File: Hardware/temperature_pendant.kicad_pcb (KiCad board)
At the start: 2 copper layers, 26.7 x 24.1 mm, 5 parts, among them J1 CONN-6, SW1 SW-MOM, U1 BLINKM/MINM, U2 TMP3X

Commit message: Added drill hole
Added a mechanical hole that could be used for chain for the pendant.
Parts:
- added MECH-HOLE220: VAL**, MECH-HOLE220, F.Cu at (213.4, 125.7)
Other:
- board size 26.7 x 24.1 mm -> 26.7 x 27.9 mm
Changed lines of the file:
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@@
     (area 199.339999 118.876 226.559 151.180001)
     (thickness 1.6)
-    (drawings 6)
+    (drawings 10)
     (tracks 36)
     (zones 0)
-    (modules 5)
+    (modules 6)
     (nets 7)
   )
@@
     )
   )
+  (module MECH-HOLE220 (layer F.Cu)
+    (at 213.36 125.73)
+    (fp_text reference MECH-HOLE220 (at 0 0) (layer F.SilkS) hide
+      (effects (font (size 1 1) (thickness 0.15)))
+    )
+    (fp_text value VAL** (at 0 0) (layer F.SilkS) hide
+      (effects (font (size 1 1) (thickness 0.15)))
+    )
+    (fp_circle (center 0 0) (end 2.5 0) (layer F.SilkS) (width 0.15))
+    (pad "" thru_hole circle (at 0 0) (size 2.8 2.8) (drill 2.2)
+      (layers *.Cu *.Mask F.SilkS)
+    )
+  )
+  (gr_line (start 199.39 123.19) (end 199.39 124.46) (angle 90) (layer Edge.Cuts) (width 0.1))
+  (gr_line (start 226.06 123.19) (end 226.06 124.46) (angle 90) (layer Edge.Cuts) (width 0.1))
+  (gr_line (start 199.39 124.46) (end 199.39 127) (angle 90) (layer Edge.Cuts) (width 0.1))
+  (gr_line (start 226.06 127) (end 226.06 124.46) (angle 90) (layer Edge.Cuts) (width 0.1))
   (gr_text "Matthew Nelson\n2013" (at 219.71 137.16) (layer F.SilkS)
     (effects (font (size 1 1) (thickness 0.25)))
@@
   (gr_line (start 226.06 151.13) (end 199.39 151.13) (angle 90) (layer Edge.Cuts) (width 0.1))
   (gr_line (start 226.06 127) (end 226.06 151.13) (angle 90) (layer Edge.Cuts) (width 0.1))
-  (gr_line (start 199.39 127) (end 226.06 127) (angle 90) (layer Edge.Cuts) (width 0.1))
+  (gr_line (start 199.39 123.19) (end 226.06 123.19) (angle 90) (layer Edge.Cuts) (width 0.1))
   (segment (start 222.78 135.345) (end 222.78 135.7981) (width 0.254) (layer F.Cu) (net 1))
   (segment (start 222.78 135.7981) (end 222.78 136.2513) (width 0.254) (layer F.Cu) (net 1))

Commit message: Fixed sensor, added locking connector
Fixed the backward wiring on the sensor, added locking connector.  Fixes
issue #4 for the sensor and issue #3 for the locking connector.
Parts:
- removed MECH-HOLE220: VAL**, MECH-HOLE220
- J1: footprint HDRV6W38P254_6X1 -> HDRV5W38P254_6X1-LOCK
- U2: footprint TO92 -> TO92-INVERT
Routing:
- net +BATT: track 53.2 -> 44.6 mm
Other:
- board text added: "Temp Pendant r2"
- board text removed: "Temp Pendant r1"

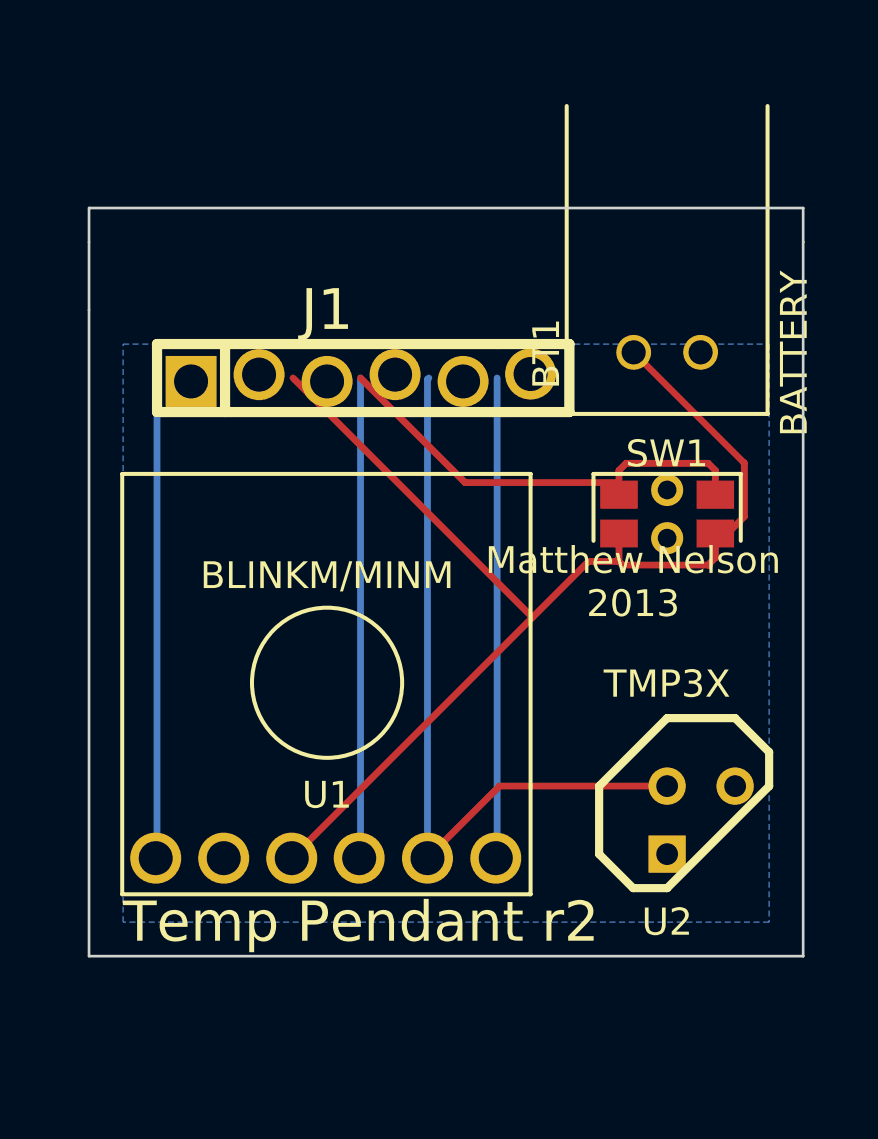
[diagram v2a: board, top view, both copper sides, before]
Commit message: Minor change cleanup
Moved switch and battery connector.  Cleaned up tracks in preparation
for a redo on the layout.
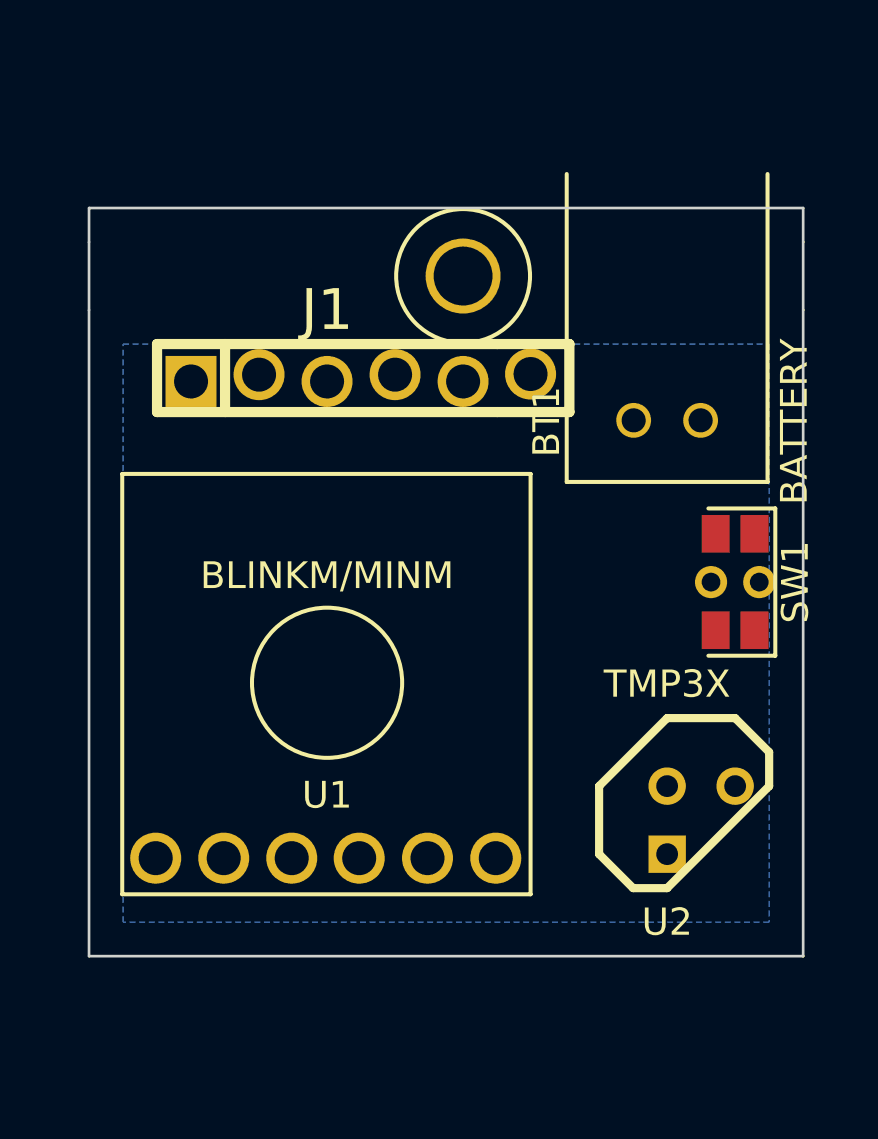
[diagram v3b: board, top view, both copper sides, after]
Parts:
- added MECH-HOLE220: VAL**, MECH-HOLE220, F.Cu at (213.4, 125.7)
- moved SW1 3.59 mm to (223.5, 137.2), turned to 270 degrees
- moved BT1 2.54 mm to (221.0, 121.9)
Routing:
- net +BATT: track 44.6 -> 0.00 mm
- net SW: track 34.8 -> 0.00 mm
- net TEMP: track 28.0 -> 0.00 mm
- net RST: track 18.0 -> 0.00 mm
- net MISO: track 18.0 -> 0.00 mm
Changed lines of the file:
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@@
   (general
     (links 15)
-    (no_connects 9)
+    (no_connects 12)
     (area 199.339999 118.876 226.559 151.180001)
     (thickness 1.6)
     (drawings 10)
-    (tracks 33)
+    (tracks 0)
     (zones 0)
-    (modules 5)
+    (modules 6)
     (nets 7)
   )
@@
   )
   (module CONN-JST-XH-2 (layer F.Cu)
-    (at 220.98 119.38)
+    (at 220.98 121.92)
     (fp_text reference BT1 (at -4.5 9.25 90) (layer F.SilkS)
       (effects (font (size 1 1) (thickness 0.15)))
@@
   )
   (module SW-EVQP7 (layer F.Cu)
-    (at 220.98 134.62)
+    (at 223.52 137.16 270)
     (descr "SW, Mom, SMD Right")
-    (fp_text reference SW1 (at 0 -2.25) (layer F.SilkS)
-      (effects (font (size 1 1) (thickness 0.15)))
-    )
-    (fp_text value SW-MOM (at 0 0) (layer F.SilkS) hide
+    (fp_text reference SW1 (at 0 -2.25 270) (layer F.SilkS)
+      (effects (font (size 1 1) (thickness 0.15)))
+    )
+    (fp_text value SW-MOM (at 0 0 270) (layer F.SilkS) hide
       (effects (font (size 1 1) (thickness 0.15)))
     )
@@
     (fp_line (start -2.75 -1.5) (end 2.75 -1.5) (layer F.SilkS) (width 0.15))
     (fp_line (start 2.75 -1.5) (end 2.75 1) (layer F.SilkS) (width 0.15))
-    (pad 1 smd rect (at 1.8 -0.725) (size 1.4 1.05)
+    (pad 1 smd rect (at 1.8 -0.725 270) (size 1.4 1.05)
       (layers F.Cu F.Paste F.Mask)
       (net 5 SW)
     )
-    (pad 1 smd rect (at -1.8 -0.725) (size 1.4 1.05)
+    (pad 1 smd rect (at -1.8 -0.725 270) (size 1.4 1.05)
       (layers F.Cu F.Paste F.Mask)
       (net 5 SW)
     )
-    (pad 2 smd rect (at -1.8 0.725) (size 1.4 1.05)
+    (pad 2 smd rect (at -1.8 0.725 270) (size 1.4 1.05)
       (layers F.Cu F.Paste F.Mask)
       (net 1 +BATT)
     )
-    (pad 2 smd rect (at 1.8 0.725) (size 1.4 1.05)
+    (pad 2 smd rect (at 1.8 0.725 270) (size 1.4 1.05)
       (layers F.Cu F.Paste F.Mask)
       (net 1 +BATT)
     )
-    (pad "" thru_hole circle (at 0 -0.9) (size 1.2 1.2) (drill 0.7)
-      (layers *.Cu *.Mask F.SilkS)
-    )
-    (pad "" thru_hole circle (at 0 0.9) (size 1.2 1.2) (drill 0.7)
+    (pad "" thru_hole circle (at 0 -0.9 270) (size 1.2 1.2) (drill 0.7)
+      (layers *.Cu *.Mask F.SilkS)
+    )
+    (pad "" thru_hole circle (at 0 0.9 270) (size 1.2 1.2) (drill 0.7)
       (layers *.Cu *.Mask F.SilkS)
     )
@@
     )
   )
+  (module MECH-HOLE220 (layer F.Cu)
+    (at 213.36 125.73)
+    (fp_text reference MECH-HOLE220 (at 0 0) (layer F.SilkS) hide
+      (effects (font (size 1 1) (thickness 0.15)))
+    )
+    (fp_text value VAL** (at 0 0) (layer F.SilkS) hide
+      (effects (font (size 1 1) (thickness 0.15)))
+    )
+    (fp_circle (center 0 0) (end 2.5 0) (layer F.SilkS) (width 0.15))
+    (pad "" thru_hole circle (at 0 0) (size 2.8 2.8) (drill 2.2)
+      (layers *.Cu *.Mask F.SilkS)
+    )
+  )
   (gr_line (start 199.39 123.19) (end 199.39 124.46) (angle 90) (layer Edge.Cuts) (width 0.1))
   (gr_line (start 226.06 123.19) (end 226.06 124.46) (angle 90) (layer Edge.Cuts) (width 0.1))
   (gr_line (start 199.39 124.46) (end 199.39 127) (angle 90) (layer Edge.Cuts) (width 0.1))
   (gr_line (start 226.06 127) (end 226.06 124.46) (angle 90) (layer Edge.Cuts) (width 0.1))
-  (gr_text "Matthew Nelson\n2013" (at 219.71 137.16) (layer F.SilkS)
-    (effects (font (size 1 1) (thickness 0.25)))
-  )
-  (gr_text "Temp Pendant r2" (at 209.55 149.86) (layer F.SilkS)
-    (effects (font (size 1.5 1.5) (thickness 0.3)))
+  (gr_text "Matthew Nelson\n2013" (at 212.09 133.35) (layer B.SilkS)
+    (effects (font (size 1 1) (thickness 0.25)) (justify mirror))
+  )
+  (gr_text "Temp Pendant r2" (at 212.09 138.43) (layer B.SilkS)
+    (effects (font (size 1.5 1.5) (thickness 0.3)) (justify mirror))
   )
   (gr_line (start 199.39 151.13) (end 199.39 127) (angle 90) (layer Edge.Cuts) (width 0.1))
@@
   (gr_line (start 226.06 127) (end 226.06 151.13) (angle 90) (layer Edge.Cuts) (width 0.1))
   (gr_line (start 199.39 123.19) (end 226.06 123.19) (angle 90) (layer Edge.Cuts) (width 0.1))
-  (segment (start 222.78 135.345) (end 222.78 135.7981) (width 0.254) (layer F.Cu) (net 1))
-  (segment (start 222.78 135.7981) (end 222.78 136.2513) (width 0.254) (layer F.Cu) (net 1))
-  (segment (start 223.8614 132.7114) (end 219.73 128.58) (width 0.254) (layer F.Cu) (net 1))
-  (segment (start 223.8614 134.7167) (end 223.8614 132.7114) (width 0.254) (layer F.Cu) (net 1))
-  (segment (start 222.78 135.7981) (end 223.8614 134.7167) (width 0.254) (layer F.Cu) (net 1))
-  (segment (start 219.18 135.345) (end 219.18 136.2513) (width 0.254) (layer F.Cu) (net 1))
-  (segment (start 222.557 136.4743) (end 222.557 136.5297) (width 0.254) (layer F.Cu) (net 1))
-  (segment (start 222.78 136.2513) (end 222.557 136.4743) (width 0.254) (layer F.Cu) (net 1))
-  (segment (start 219.18 136.3905) (end 219.18 136.2513) (width 0.254) (layer F.Cu) (net 1))
-  (segment (start 219.3192 136.5297) (end 219.18 136.3905) (width 0.254) (layer F.Cu) (net 1))
-  (segment (start 222.557 136.5297) (end 219.3192 136.5297) (width 0.254) (layer F.Cu) (net 1))
-  (segment (start 215.95 138.48) (end 207.01 129.54) (width 0.254) (layer F.Cu) (net 1))
-  (segment (start 218.0395 136.3905) (end 215.95 138.48) (width 0.254) (layer F.Cu) (net 1))
-  (segment (start 219.18 136.3905) (end 218.0395 136.3905) (width 0.254) (layer F.Cu) (net 1))
-  (segment (start 215.95 138.48) (end 206.96 147.47) (width 0.254) (layer F.Cu) (net 1))
-  (segment (start 214.63 147.42) (end 214.63 129.54) (width 0.254) (layer B.Cu) (net 3))
-  (segment (start 214.58 147.47) (end 214.63 147.42) (width 0.254) (layer B.Cu) (net 3))
-  (segment (start 201.93 147.42) (end 201.93 129.54) (width 0.254) (layer B.Cu) (net 4))
-  (segment (start 201.88 147.47) (end 201.93 147.42) (width 0.254) (layer B.Cu) (net 4))
-  (segment (start 222.5154 132.7241) (end 222.78 132.9887) (width 0.254) (layer F.Cu) (net 5))
-  (segment (start 219.4446 132.7241) (end 222.5154 132.7241) (width 0.254) (layer F.Cu) (net 5))
-  (segment (start 219.18 132.9887) (end 219.4446 132.7241) (width 0.254) (layer F.Cu) (net 5))
-  (segment (start 222.78 133.895) (end 222.78 132.9887) (width 0.254) (layer F.Cu) (net 5))
-  (segment (start 219.18 133.895) (end 219.18 133.4418) (width 0.254) (layer F.Cu) (net 5))
-  (segment (start 219.18 133.4418) (end 219.18 132.9887) (width 0.254) (layer F.Cu) (net 5))
-  (segment (start 213.4318 133.4418) (end 209.53 129.54) (width 0.254) (layer F.Cu) (net 5))
-  (segment (start 219.18 133.4418) (end 213.4318 133.4418) (width 0.254) (layer F.Cu) (net 5))
-  (segment (start 209.53 147.42) (end 209.53 129.54) (width 0.254) (layer B.Cu) (net 5))
-  (segment (start 209.48 147.47) (end 209.53 147.42) (width 0.254) (layer B.Cu) (net 5))
-  (segment (start 214.72 144.78) (end 220.98 144.78) (width 0.254) (layer F.Cu) (net 6))
-  (segment (start 212.03 147.47) (end 214.72 144.78) (width 0.254) (layer F.Cu) (net 6))
-  (segment (start 212.03 129.59) (end 212.03 147.47) (width 0.254) (layer B.Cu) (net 6))
-  (segment (start 212.08 129.54) (end 212.03 129.59) (width 0.254) (layer B.Cu) (net 6))
   (zone (net 2) (net_name GND) (layer B.Cu) (hatch edge 0.508)
     (connect_pads (clearance 0.16))

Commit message: Final cleanup and new routed board
Re-routed board based on new placement
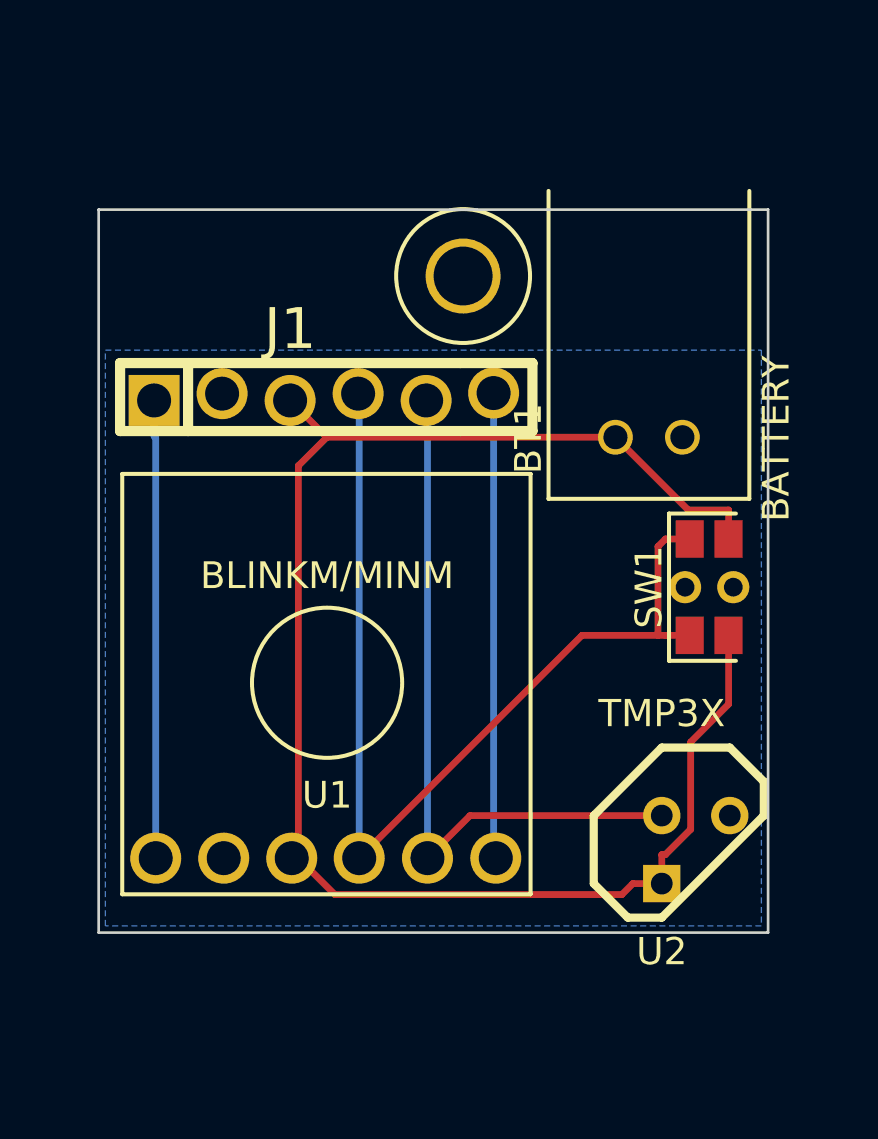
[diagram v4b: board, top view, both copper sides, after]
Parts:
- moved J1 1.55 mm to (206.9, 130.2)
- moved U2 1.12 mm to (222.1, 147.2)
- moved SW1 0.99 mm to (222.6, 137.3), turned to 90 degrees
- moved BT1 0.93 mm to (220.3, 122.5)
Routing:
- net +BATT: track 0.00 -> 60.2 mm
- net SW: track 0.00 -> 37.8 mm
- net TEMP: track 0.00 -> 26.5 mm
- net MISO: track 0.00 -> 17.4 mm
- net RST: track 0.00 -> 17.1 mm
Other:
- board size 26.7 x 27.9 mm -> 25 x 27 mm

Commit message: Updated PCB
Updated PCB with changes done to schematic.  made the board longer but
not as wide.
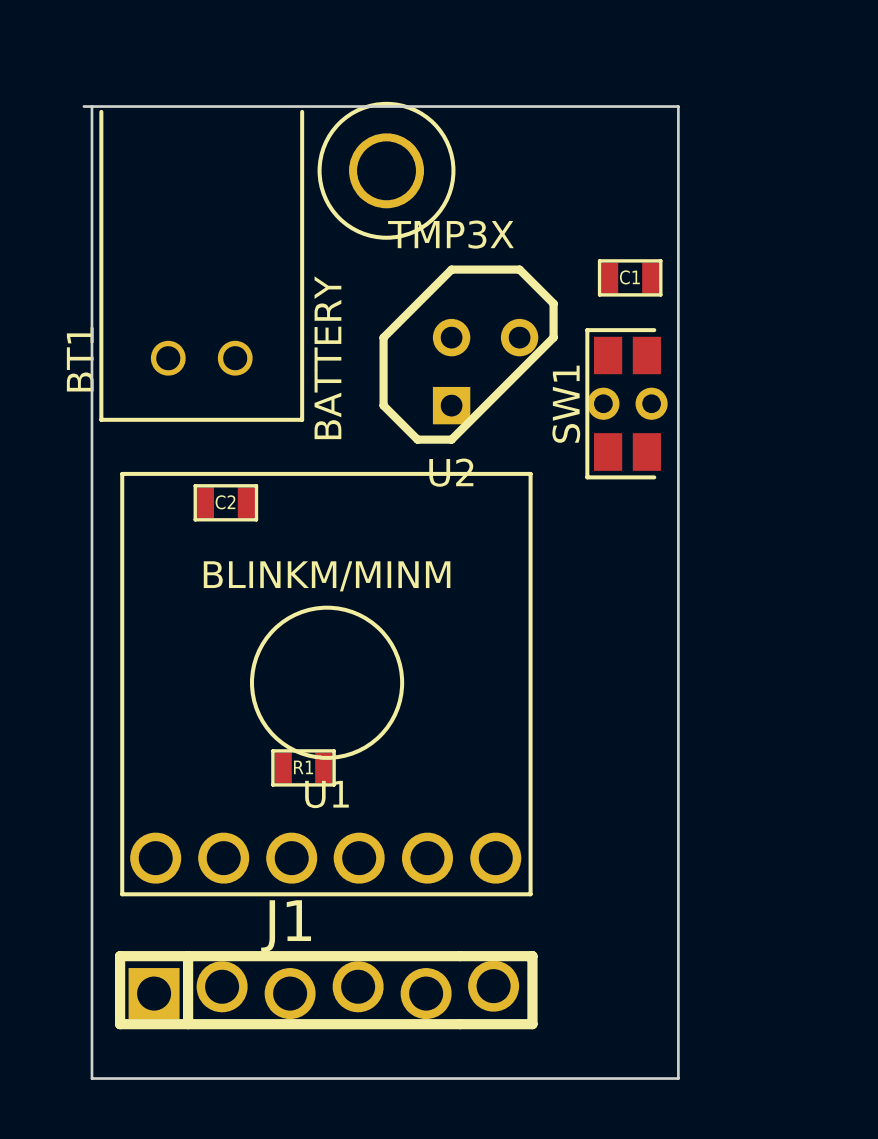
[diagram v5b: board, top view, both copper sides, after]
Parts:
- added C1: .1 uF, SM0603, F.Cu at (219.6, 125.8)
- added C2: .1 uF, SM0603, F.Cu at (204.5, 134.2)
- added R1: 10k, SM0603, F.Cu at (207.4, 144.1)
- moved J1 22.2 mm to (206.9, 152.4)
- moved U2 19.5 mm to (214.2, 129.3)
- moved BT1 17.0 mm to (203.6, 119.6)
- moved SW1 7.50 mm to (219.5, 130.5)
- moved MECH-HOLE220 4.86 mm to (210.5, 121.8)
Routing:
- net +BATT: track 60.2 -> 0.00 mm
- net SW: track 37.8 -> 0.00 mm
- net TEMP: track 26.5 -> 0.00 mm
- net MISO: track 17.4 -> 0.00 mm
- net RST: track 17.1 -> 0.00 mm
- removed copper zone on B.Cu, net GND
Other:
- board size 25 x 27 mm -> 22.2 x 36.3 mm

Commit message: updated PCB
Updated PCB layout with new charger and a few other changes to packages.
Swapped out JST connector for the smaller PH series.
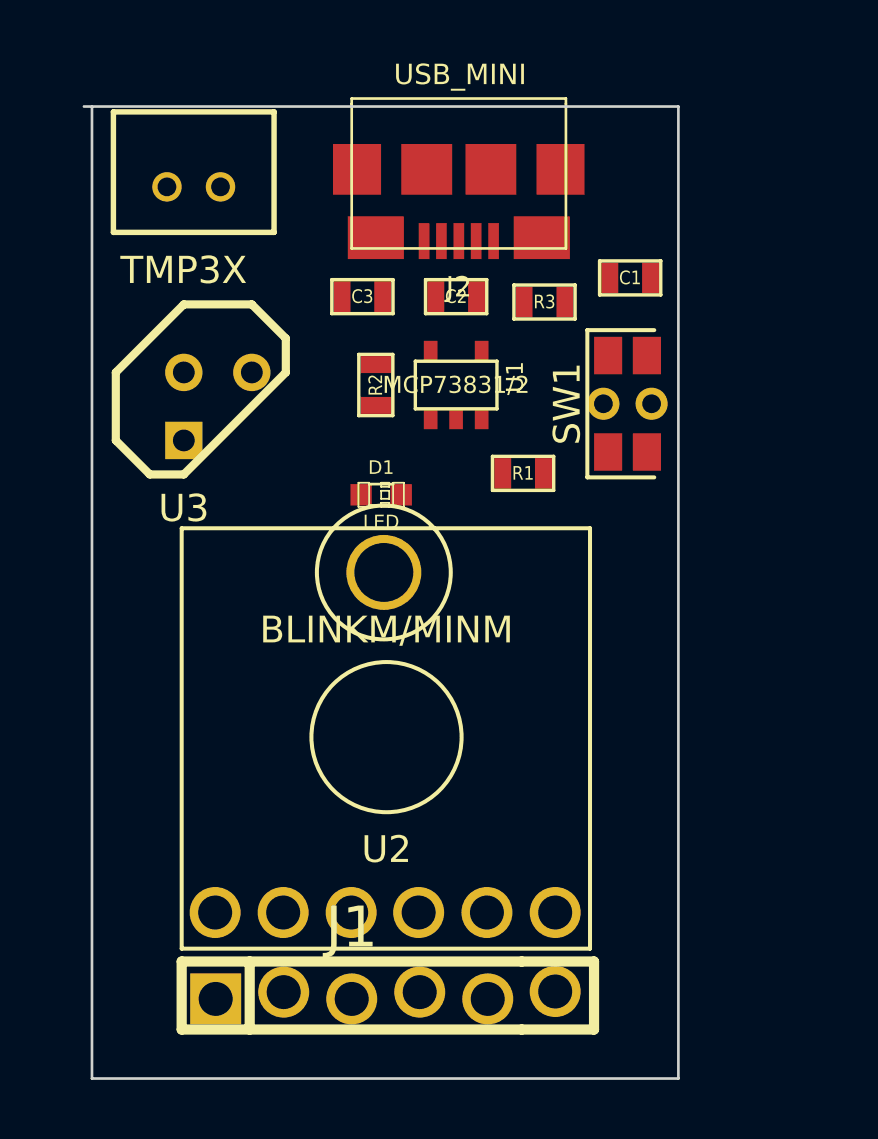
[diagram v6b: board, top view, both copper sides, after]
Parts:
- added C3: .1 uF, SM0603, F.Cu at (209.6, 126.5)
- added D1: LED, LED-0603, F.Cu at (210.3, 133.9)
- added J2: USB_MINI, USB_MICRO_B, F.Cu at (213.2, 120.3)
- added R2: 2K, SM0603, F.Cu at (210.1, 129.8)
- added R3: 10k, SM0603, F.Cu at (216.4, 126.7)
- added U3: TMP3X, TO92-INVERT, F.Cu at (204.2, 130.6)
- BT1: footprint CONN-JST-XH-2 -> CONN-JST-PH-2V
- C2: value .1 uF -> 4.7uF
- R1: value 10k -> 330
- U1: value BLINKM/MINM -> MCP73831/2; footprint BlinkM -> SOT23-5
- U2: value TMP3X -> BLINKM/MINM; footprint TO92-INVERT -> BlinkM
- moved MECH-HOLE220 15.0 mm to (210.4, 136.8)
- moved U2 14.2 mm to (210.5, 143.0)
- moved R1 13.7 mm to (215.6, 133.1)
- moved U1 12.2 mm to (213.1, 129.8)
- moved C2 11.5 mm to (213.1, 126.5)
- moved BT1 2.82 mm to (203.3, 122.4)
- moved J1 2.31 mm to (209.2, 152.6)
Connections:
- C2 pad 1: GND -> N-000008
- C2 pad 2: +BATT -> GND
- R1 pad 1: SW -> N-000006
- R1 pad 2: GND -> N-000008
- U1 pad 1: RST -> N-000007
- U1 pad 4: SW -> N-000008
- U1 pad 5: TEMP -> N-000001
- U2 pad 1: +BATT -> RST
- U2 pad 2: TEMP -> GND
- U2 pad 3: GND -> +BATT
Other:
- board text added: "Temp Pendant r3"
- board text removed: "Temp Pendant r2"
